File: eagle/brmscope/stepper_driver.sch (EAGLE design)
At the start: 34 parts, among them IC1 ULN2074BN, IC2 ULN2074BN, IC3 ULN2074BN, IC4 MEGA8-AI, J1 POWER_JACKPTH, Q1 16 MHz, X1 USBPTH

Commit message: INT0 connected to D+ line (USBasploader requirement)
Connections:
- net N$4: now also IC4.PD2(INT0)
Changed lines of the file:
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@@
 <pinref part="IC4" gate="G$1" pin="PC0(ADC0)"/>
 <wire x1="-40.64" y1="40.64" x2="-43.18" y2="40.64" width="0.1524" layer="91"/>
+<pinref part="IC4" gate="G$1" pin="PD2(INT0)"/>
+<wire x1="-43.18" y1="12.7" x2="-40.64" y2="12.7" width="0.1524" layer="91"/>
+<wire x1="-40.64" y1="12.7" x2="-40.64" y2="40.64" width="0.1524" layer="91"/>
+<junction x="-40.64" y="40.64"/>
 </segment>
 </net>

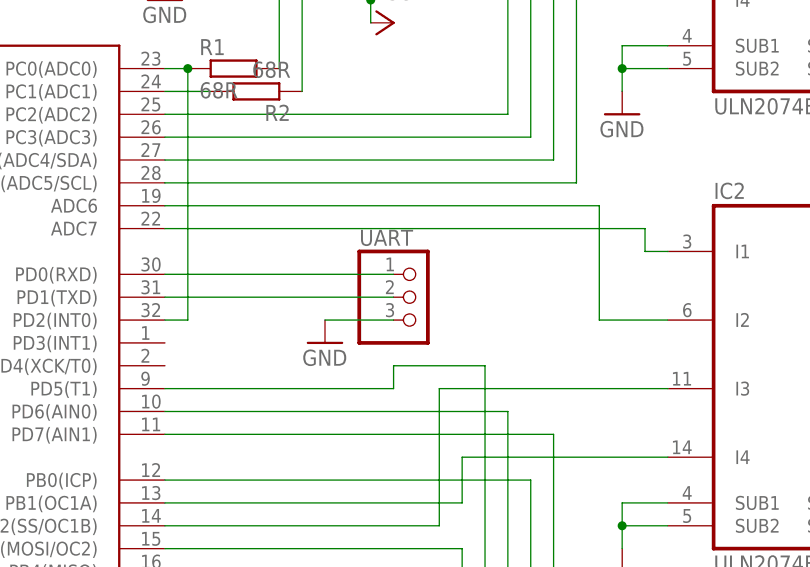
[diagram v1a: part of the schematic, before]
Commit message: board corrections + atmega firmware
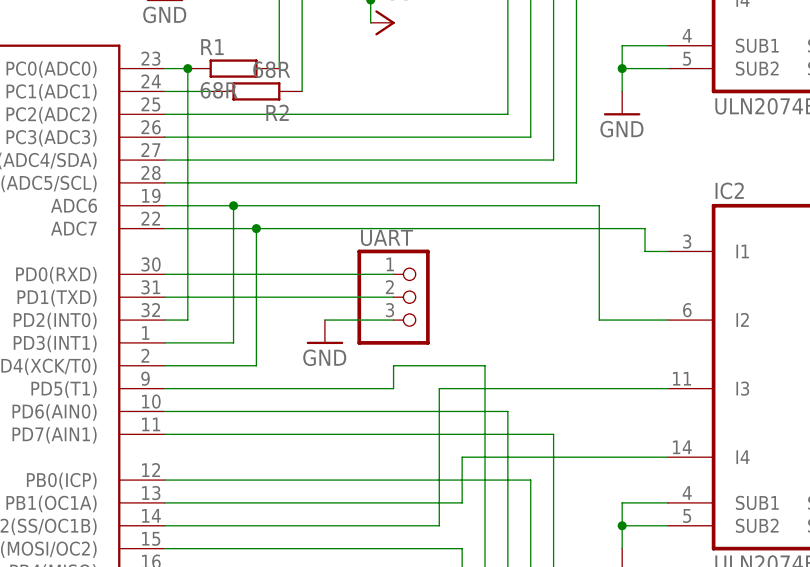
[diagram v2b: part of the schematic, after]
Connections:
- net N$12: now also IC4.PD3(INT1)
- net N$13: now also IC4.PD4(XCK/T0)
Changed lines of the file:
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@@
 <segment>
 <pinref part="IC4" gate="G$1" pin="ADC7"/>
-<wire x1="-43.18" y1="22.86" x2="10.16" y2="22.86" width="0.1524" layer="91"/>
+<wire x1="-43.18" y1="22.86" x2="-33.02" y2="22.86" width="0.1524" layer="91"/>
 <pinref part="IC2" gate="A" pin="I1"/>
+<wire x1="-33.02" y1="22.86" x2="10.16" y2="22.86" width="0.1524" layer="91"/>
 <wire x1="10.16" y1="22.86" x2="10.16" y2="20.32" width="0.1524" layer="91"/>
 <wire x1="10.16" y1="20.32" x2="12.7" y2="20.32" width="0.1524" layer="91"/>
+<pinref part="IC4" gate="G$1" pin="PD4(XCK/T0)"/>
+<wire x1="-43.18" y1="7.62" x2="-33.02" y2="7.62" width="0.1524" layer="91"/>
+<wire x1="-33.02" y1="7.62" x2="-33.02" y2="22.86" width="0.1524" layer="91"/>
+<junction x="-33.02" y="22.86"/>
 </segment>
 </net>
@@
 <segment>
 <pinref part="IC4" gate="G$1" pin="ADC6"/>
-<wire x1="-43.18" y1="25.4" x2="5.08" y2="25.4" width="0.1524" layer="91"/>
+<wire x1="-43.18" y1="25.4" x2="-35.56" y2="25.4" width="0.1524" layer="91"/>
 <pinref part="IC2" gate="A" pin="I2"/>
+<wire x1="-35.56" y1="25.4" x2="5.08" y2="25.4" width="0.1524" layer="91"/>
 <wire x1="5.08" y1="25.4" x2="5.08" y2="12.7" width="0.1524" layer="91"/>
 <wire x1="5.08" y1="12.7" x2="12.7" y2="12.7" width="0.1524" layer="91"/>
-</segment>
-</net>
+<pinref part="IC4" gate="G$1" pin="PD3(INT1)"/>
+<wire x1="-43.18" y1="10.16" x2="-35.56" y2="10.16" width="0.1524" layer="91"/>
+<wire x1="-35.56" y1="10.16" x2="-35.56" y2="25.4" width="0.1524" layer="91"/>
+<junction x="-35.56" y="25.4"/>
+</segment>
+</net>
